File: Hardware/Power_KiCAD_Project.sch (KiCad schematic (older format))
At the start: 7 parts, among them J1 XT60-M, J2 XT60-M, J3 XT60-M, J4 XT60-M, J5 XT60-M, J6 PJ-102AH, J8 XT60-M

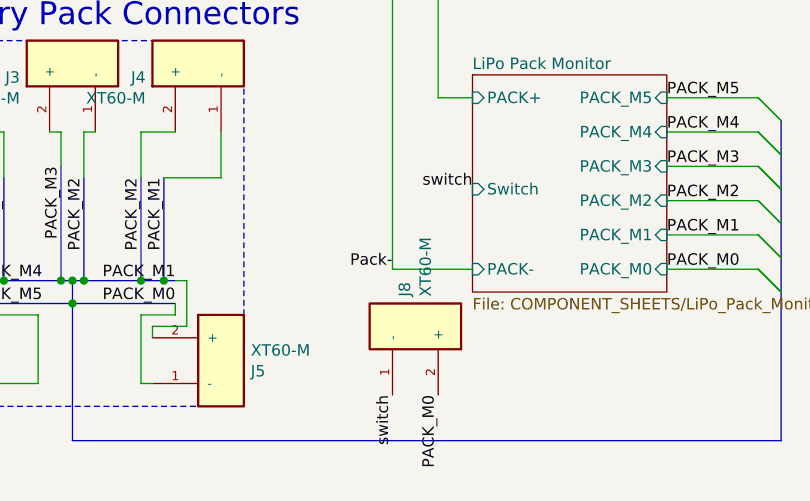
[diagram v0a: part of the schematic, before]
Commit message: FIxed board
issues with the board after the merge have been fixed
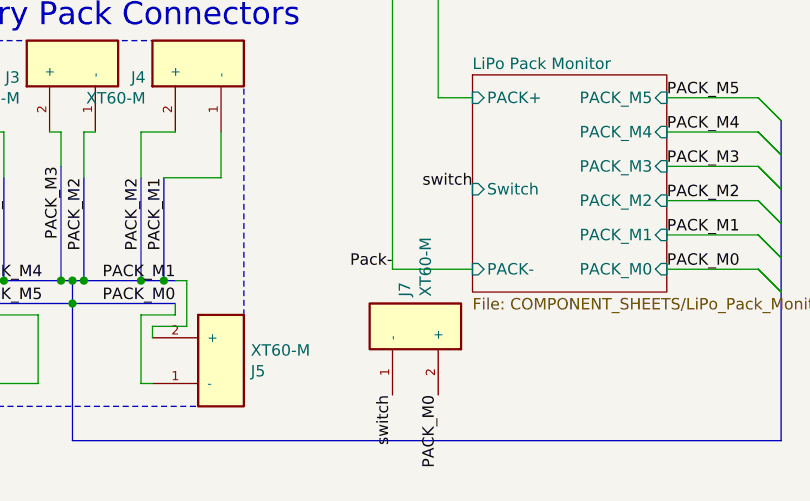
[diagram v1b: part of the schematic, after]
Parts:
- renumbered J8 to J7
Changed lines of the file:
@@
 $EndDescr
 $Comp
-L power:+3.3V #PWR03
+L power:+3.3V #PWR01
 U 1 1 61B3C742
 P 4750 1150
-F 0 "#PWR03" H 4750 1000 50  0001 C CNN
+F 0 "#PWR01" H 4750 1000 50  0001 C CNN
 F 1 "+3.3V" H 4765 1323 50  0000 C CNN
 F 2 "" H 4750 1150 50  0001 C CNN
@@
 	3550 4800 3550 5800
 $Comp
-L power:+3.3V #PWR02
+L power:+3.3V #PWR03
 U 1 1 61A5452E
 P 5050 4500
-F 0 "#PWR02" H 5050 4350 50  0001 C CNN
+F 0 "#PWR03" H 5050 4350 50  0001 C CNN
 F 1 "+3.3V" H 5065 4673 50  0000 C CNN
 F 2 "" H 5050 4500 50  0001 C CNN
@@
 $EndComp
 $Comp
-L power:+5V #PWR01
+L power:+5V #PWR02
 U 1 1 61A56282
 P 4800 4500
-F 0 "#PWR01" H 4800 4350 50  0001 C CNN
+F 0 "#PWR02" H 4800 4350 50  0001 C CNN
 F 1 "+5V" H 4815 4673 50  0000 C CNN
 F 2 "" H 4800 4500 50  0001 C CNN
@@
 NoConn ~ 2800 2900
 $Comp
-L Power_KiCAD_Project-rescue:XT60-M-XT60-M J8
+L Power_KiCAD_Project-rescue:XT60-M-XT60-M J7
 U 1 1 61C843A7
 P 3450 6800
-F 0 "J8" H 3580 6846 50  0000 L CNN
+F 0 "J7" H 3580 6846 50  0000 L CNN
 F 1 "XT60-M" H 3580 6755 50  0000 L CNN
 F 2 "XT60-M:AMASS_XT60-M" H 3450 6800 50  0001 L BNN

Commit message: Rearranged LiPo Monitor component sheet
 - Added XT60 connector for external switch connection
 - Updated a few component symbols to be the default ones
 - Replaced label "ground" with the GNDREF symbol
 - LiPo Pack Monitor I2C and Alert Lines still need to be added
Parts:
- removed J6: PJ-102AH, SamacSys_Parts:PJ-102AH, symbol Power_KiCAD_Project-rescue:PJ-102AH-SamacSys_Parts
- added J10: XT60 Cell 2, XT60-M:AMASS_XT60-M, symbol Power_KiCAD_Project-rescue:XT60-M-XT60-M
- added J11: XT60 Cell 1, XT60-M:AMASS_XT60-M, symbol Power_KiCAD_Project-rescue:XT60-M-XT60-M
- added J6: Barrel_Jack_MountingPin, symbol Connector:Barrel_Jack_MountingPin
- added J8: XT60 Cell 4, XT60-M:AMASS_XT60-M, symbol Power_KiCAD_Project-rescue:XT60-M-XT60-M
- added J9: XT60 Cell 3, XT60-M:AMASS_XT60-M, symbol Power_KiCAD_Project-rescue:XT60-M-XT60-M
- J7: value XT60-M -> XT60 Cell 5
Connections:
- net labels added: GNDREF
- net labels removed: Pack-, switch
- wire segments 72 -> 86
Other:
- moved on the sheet: J1, J2, J3, J4, J5

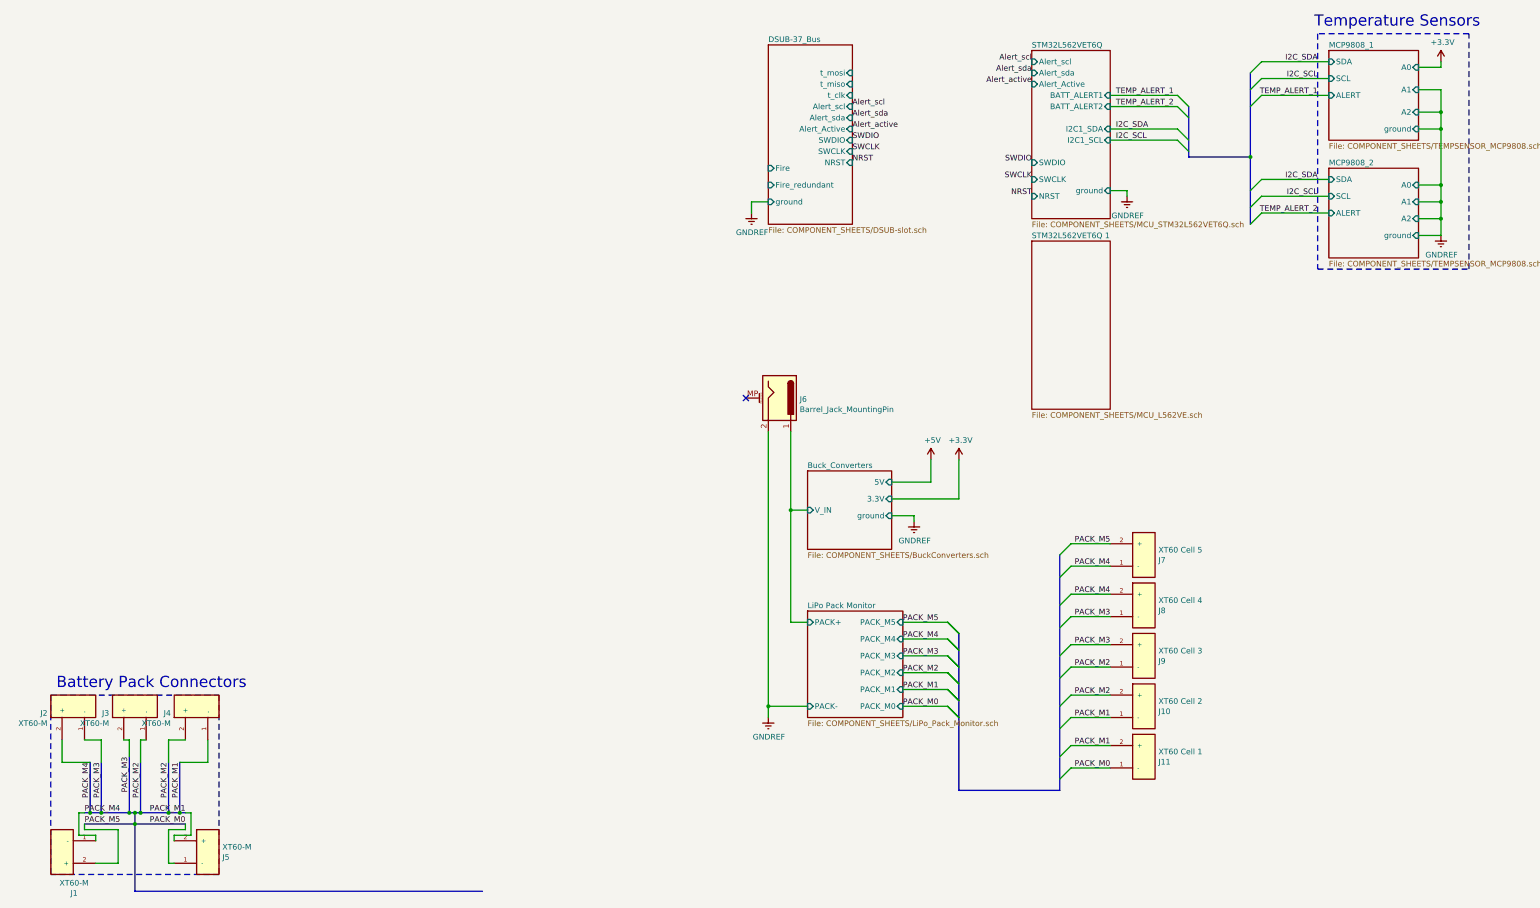
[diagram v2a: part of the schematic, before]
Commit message: Fixed ground symbols in component sheets, corrected MCU sheet
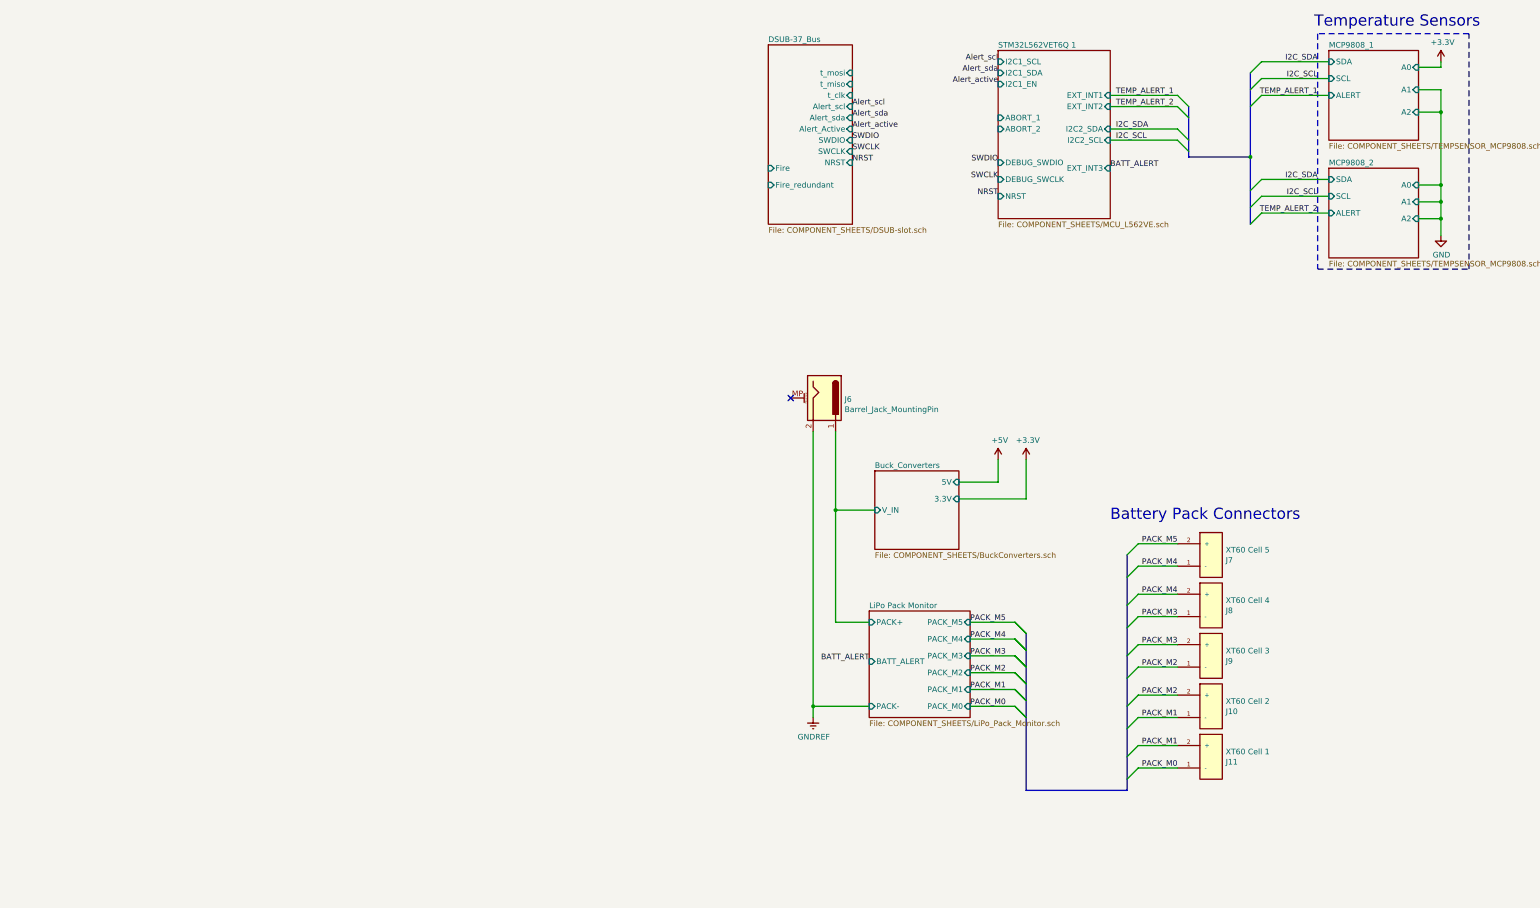
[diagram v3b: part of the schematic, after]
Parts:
- removed J1, J2, J3, J4, J5: XT60-M, XT60-M:AMASS_XT60-M, symbol Power_KiCAD_Project-rescue:XT60-M-XT60-M
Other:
- moved on the sheet: J10, J11, J6, J7, J8, J9

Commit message: Updated component footprints, moved to RDT_Custom_Footprints library
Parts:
- J10, J11, J7, J8, J9: footprint XT60-M:AMASS_XT60-M -> RDT_Custom_Footprints:AMASS_XT60-M
- J6: footprint (none) -> Connector_BarrelJack:BarrelJack_CUI_PJ-102AH_Horizontal
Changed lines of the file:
@@
-$EndSheet
-$Sheet
-S 800  850  750  1600
-U 61D3585E
-F0 "DSUB-37_Bus" 50
-F1 "COMPONENT_SHEETS/DSUB-slot.sch" 50
-F2 "t_mosi" I R 1550 1100 50
-F3 "t_miso" I R 1550 1200 50
-F4 "t_clk" I R 1550 1300 50
-F5 "Alert_scl" I R 1550 1400 50
-F6 "Alert_sda" I R 1550 1500 50
-F7 "Alert_Active" I R 1550 1600 50
-F8 "SWDIO" I R 1550 1700 50
-F9 "SWCLK" I R 1550 1800 50
-F10 "NRST" I R 1550 1900 50
-F11 "Fire" I L 800 1950 50
-F12 "Fire_redundant" I L 800 2100 50
 $EndSheet
 $Sheet
@@
 F 0 "J11" H 4880 7246 50  0000 L CNN
 F 1 "XT60 Cell 1" H 4880 7155 50  0000 L CNN
-F 2 "XT60-M:AMASS_XT60-M" H 4750 7200 50  0001 L BNN
+F 2 "RDT_Custom_Footprints:AMASS_XT60-M" H 4750 7200 50  0001 L BNN
 F 3 "" H 4750 7200 50  0001 L BNN
 F 4 "XT60-M" H 4750 7200 50  0001 L BNN "MP"
@@
 F 0 "J6" V 1311 4180 50  0000 L CNN
 F 1 "Barrel_Jack_MountingPin" V 1402 4180 50  0000 L CNN
-F 2 "" H 1350 3960 50  0001 C CNN
+F 2 "Connector_BarrelJack:BarrelJack_CUI_PJ-102AH_Horizontal" H 1350 3960 50  0001 C CNN
 F 3 "~" H 1350 3960 50  0001 C CNN
 	1    1300 4000
@@
 F 0 "J10" H 4880 6796 50  0000 L CNN
 F 1 "XT60 Cell 2" H 4880 6705 50  0000 L CNN
-F 2 "XT60-M:AMASS_XT60-M" H 4750 6750 50  0001 L BNN
+F 2 "RDT_Custom_Footprints:AMASS_XT60-M" H 4750 6750 50  0001 L BNN
 F 3 "" H 4750 6750 50  0001 L BNN
 F 4 "XT60-M" H 4750 6750 50  0001 L BNN "MP"
@@
 F 0 "J9" H 4880 6346 50  0000 L CNN
 F 1 "XT60 Cell 3" H 4880 6255 50  0000 L CNN
-F 2 "XT60-M:AMASS_XT60-M" H 4750 6300 50  0001 L BNN
+F 2 "RDT_Custom_Footprints:AMASS_XT60-M" H 4750 6300 50  0001 L BNN
 F 3 "" H 4750 6300 50  0001 L BNN
 F 4 "XT60-M" H 4750 6300 50  0001 L BNN "MP"
@@
 F 0 "J8" H 4880 5896 50  0000 L CNN
 F 1 "XT60 Cell 4" H 4880 5805 50  0000 L CNN
-F 2 "XT60-M:AMASS_XT60-M" H 4750 5850 50  0001 L BNN
+F 2 "RDT_Custom_Footprints:AMASS_XT60-M" H 4750 5850 50  0001 L BNN
 F 3 "" H 4750 5850 50  0001 L BNN
 F 4 "XT60-M" H 4750 5850 50  0001 L BNN "MP"
@@
 F 0 "J7" H 4880 5446 50  0000 L CNN
 F 1 "XT60 Cell 5" H 4880 5355 50  0000 L CNN
-F 2 "XT60-M:AMASS_XT60-M" H 4750 5400 50  0001 L BNN
+F 2 "RDT_Custom_Footprints:AMASS_XT60-M" H 4750 5400 50  0001 L BNN
 F 3 "" H 4750 5400 50  0001 L BNN
 F 4 "XT60-M" H 4750 5400 50  0001 L BNN "MP"
@@
 	6800 2550 6800 2400
 $Comp
-L power:GND #PWR?
+L power:GND #PWR0101
 U 1 1 61CCB2E2
 P 6800 2550
-F 0 "#PWR?" H 6800 2300 50  0001 C CNN
+F 0 "#PWR0101" H 6800 2300 50  0001 C CNN
 F 1 "GND" H 6805 2377 50  0000 C CNN
 F 2 "" H 6800 2550 50  0001 C CNN
@@
 Wire Wire Line
 	1400 5000 1750 5000
+$Sheet
+S 800  850  750  1600
+U 61D3585E
+F0 "DSUB-37_Bus" 50
+F1 "COMPONENT_SHEETS/DSUB-slot.sch" 50
+F2 "t_mosi" I R 1550 1100 50
+F3 "t_miso" I R 1550 1200 50
+F4 "t_clk" I R 1550 1300 50
+F5 "Alert_scl" I R 1550 1400 50
+F6 "Alert_sda" I R 1550 1500 50
+F7 "Alert_Active" I R 1550 1600 50
+F8 "SWDIO" I R 1550 1700 50
+F9 "SWCLK" I R 1550 1800 50
+F10 "NRST" I R 1550 1900 50
+F11 "Fire" I L 800 1950 50
+F12 "Fire_redundant" I L 800 2100 50
+$EndSheet
 Wire Bus Line
 	5100 1850 5100 2450

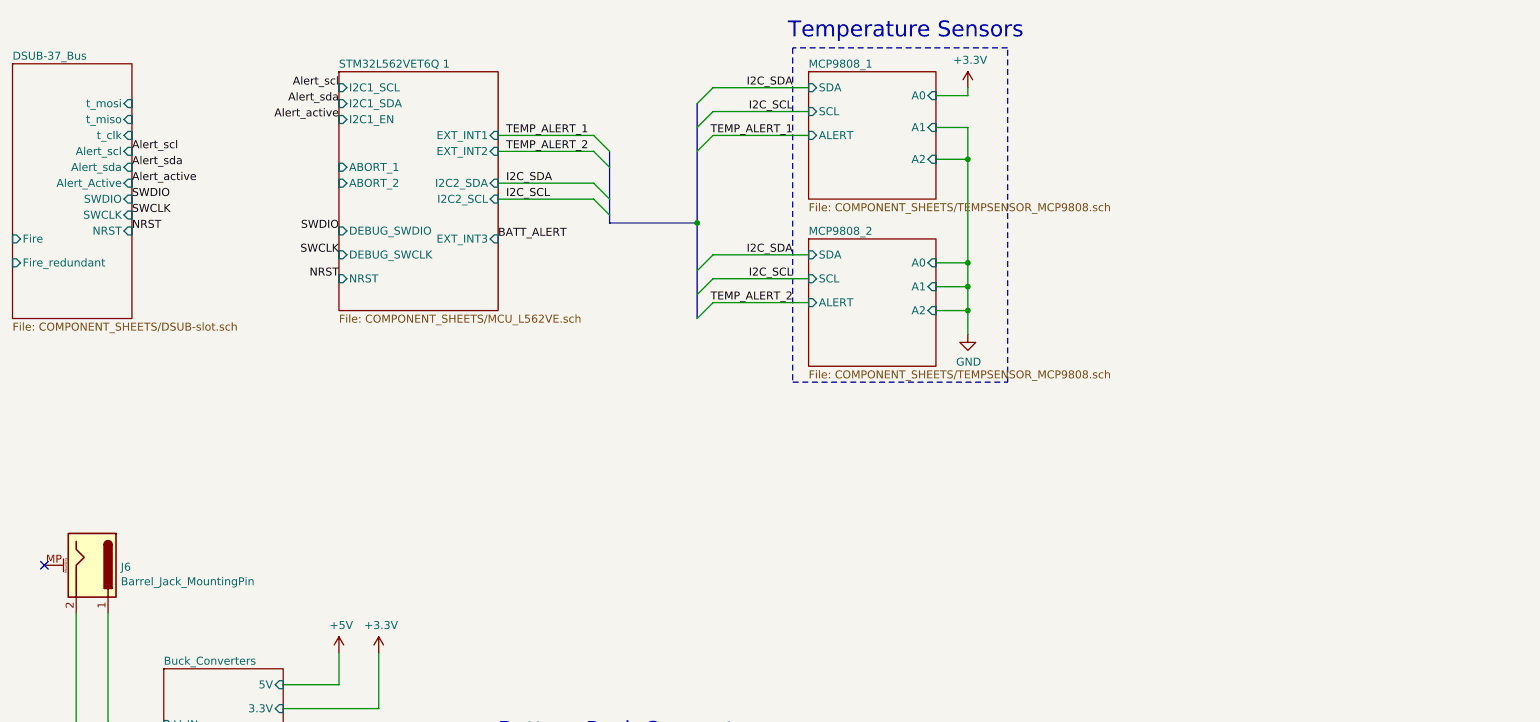
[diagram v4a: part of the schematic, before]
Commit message: Cleaned up main schematic page, connected barrel jack ground pin to GND
Is this ok? The Barrel Jack is like this right now:

Pin -> Pack+
Barrel -> GNDREF
Mounting Pin -> GND
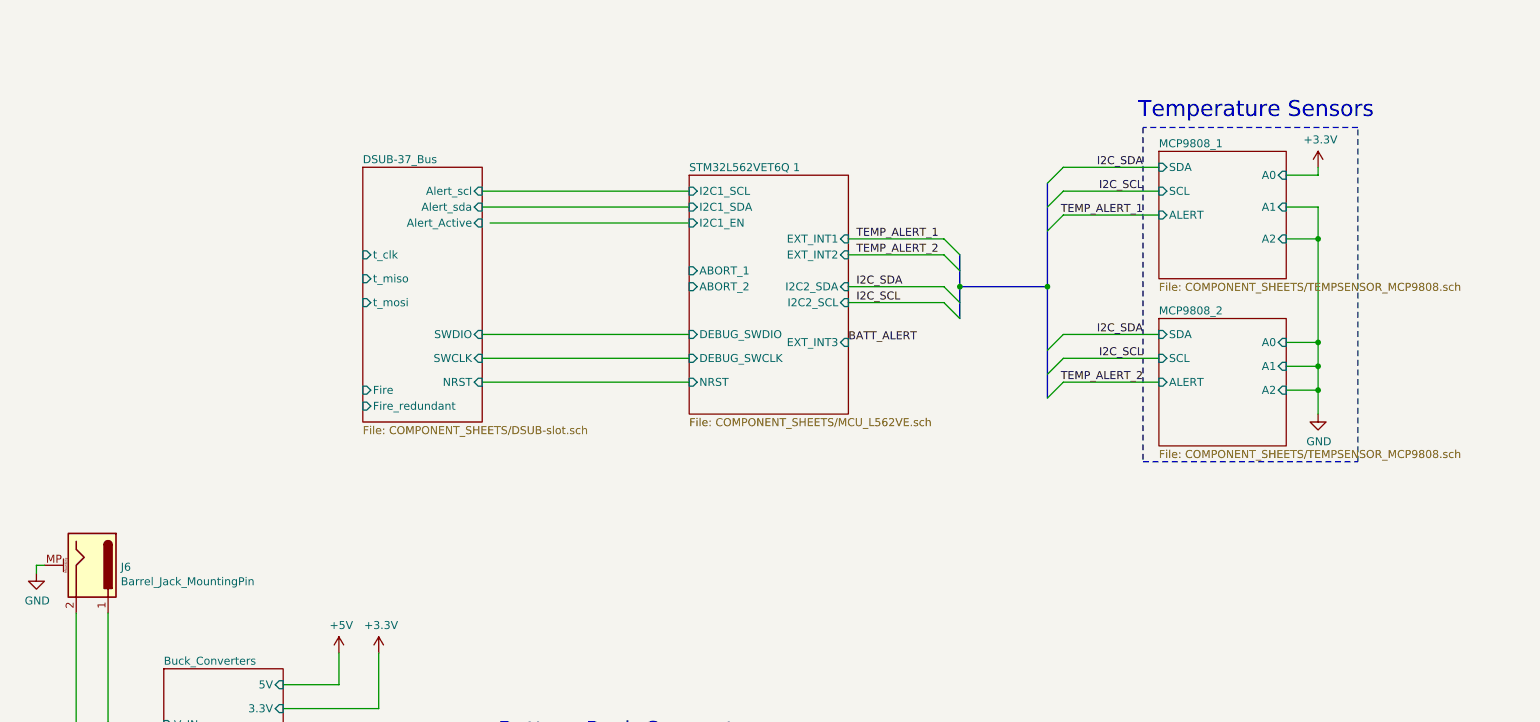
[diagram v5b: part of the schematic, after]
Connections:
- net GND: now also J6.MP (MountPin)
- no-connect marks 1 -> 0
